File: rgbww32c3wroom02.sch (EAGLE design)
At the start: 25 parts

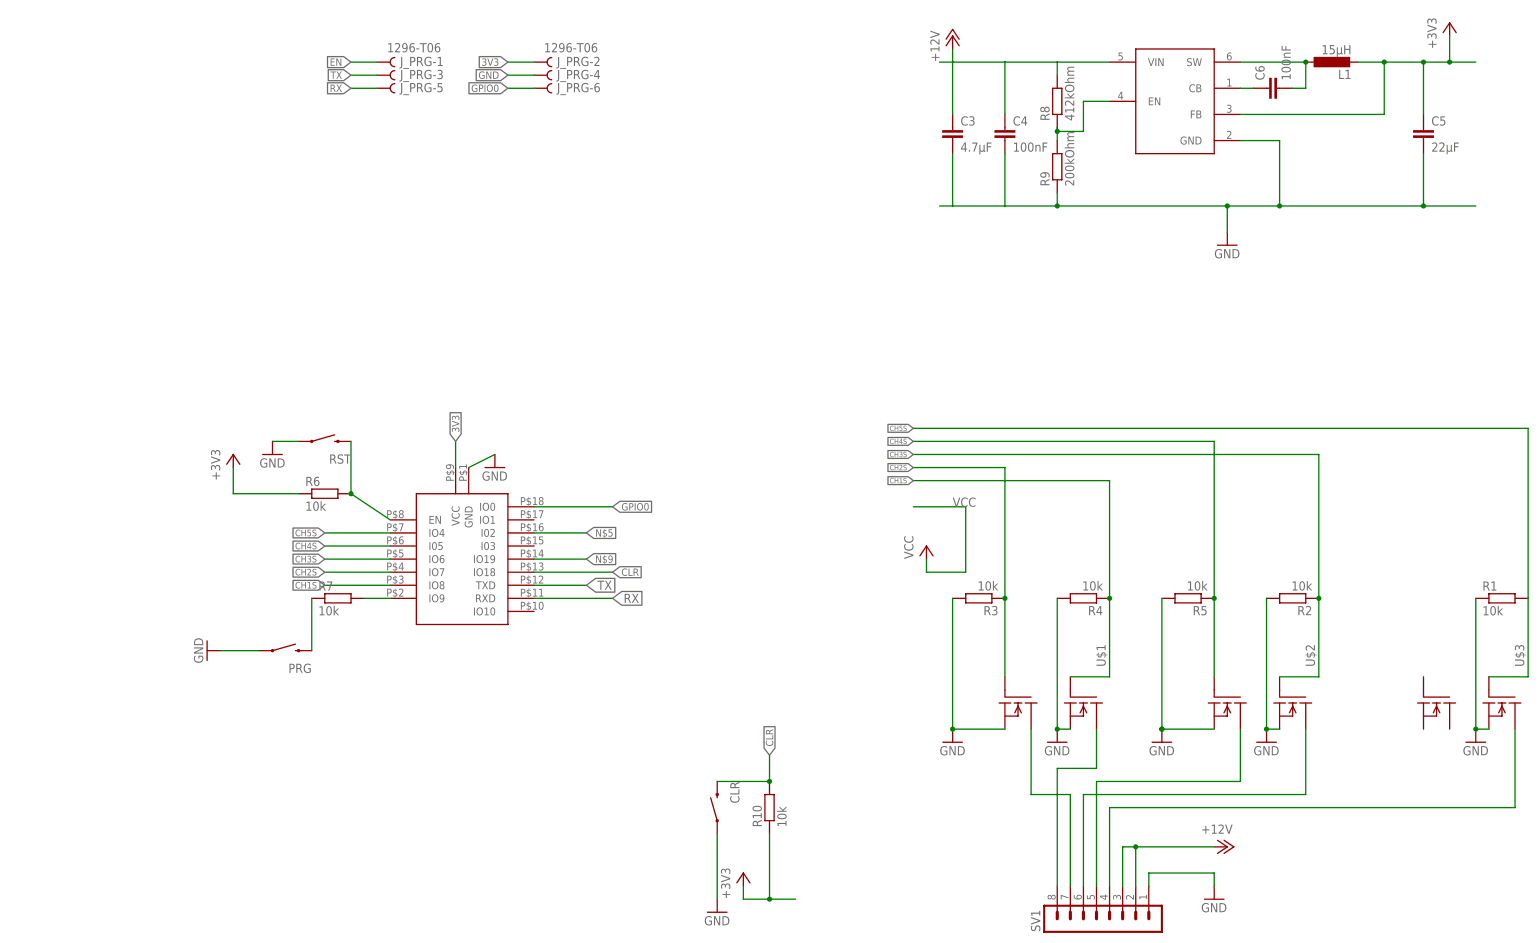
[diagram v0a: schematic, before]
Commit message: corrected PRG pin for esp32c3
sometimes, I notice things way late. Like the fact that the PRG pin on the esp32c3 is no longer GPIO0 as it was with all xtensa based chips but now it's GPIO9.
I was using GPIO9 as an output pin with a 10k pulldown which should have always set the chip into download mode - not what I wanted. I have now shuffeled pins around and this should be ok now.
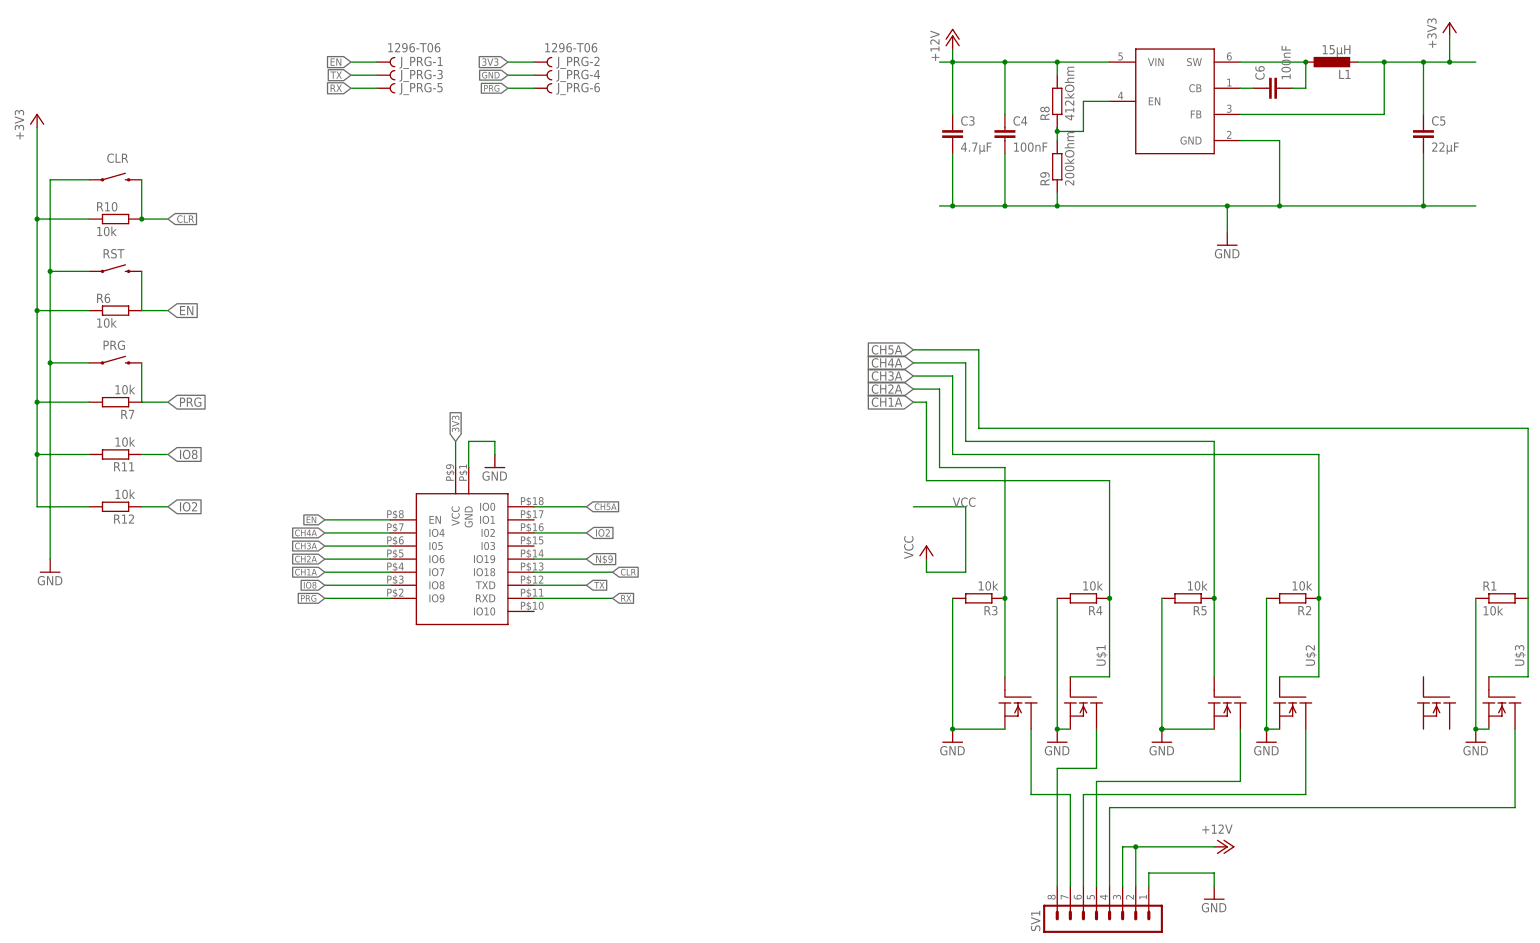
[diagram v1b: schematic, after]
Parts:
- added R11, R12: 10k, rcl:R-EU_R0805
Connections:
- removed net CH1S: R4.1, U$1.G, U$5.IO8
- removed net CH2S: R3.1, U$1.G1, U$5.IO7
- removed net CH3S: R2.1, U$2.G, U$5.IO6
- removed net CH4S: R5.1, U$2.G1, U$5.I05
- removed net CH5S: R1.2, U$3.G, U$5.IO4
- removed net GPIO0: J_PRG-6.B, U$5.IO0
- removed net N$5: U$5.I02
- removed net PRG1: PRG.2, R7.1
- new net CH1A: R4.1, U$1.G, U$5.IO7
- new net CH2A: R3.1, U$1.G1, U$5.IO6
- new net CH3A: R2.1, U$2.G, U$5.I05
- new net CH4A: R5.1, U$2.G1, U$5.IO4
- new net CH5A: R1.2, U$3.G, U$5.IO0
- new net IO2: R12.1, U$5.I02
- new net IO8: R11.1, U$5.IO8
- net 3V3: now also R11.2, R12.2, R7.2
- net PRG: now also J_PRG-6.B, PRG.2, R7.1; no longer R7.2
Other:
- moved on the sheet: CLR, PRG, R10, R6, R7, RST
